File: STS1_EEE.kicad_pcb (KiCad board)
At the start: 4 copper layers, 81.1 x 85 mm, 51 parts, among them J1 2477, U1 coordinate_system, U10 ST_Logo, U2 MP28167GQ

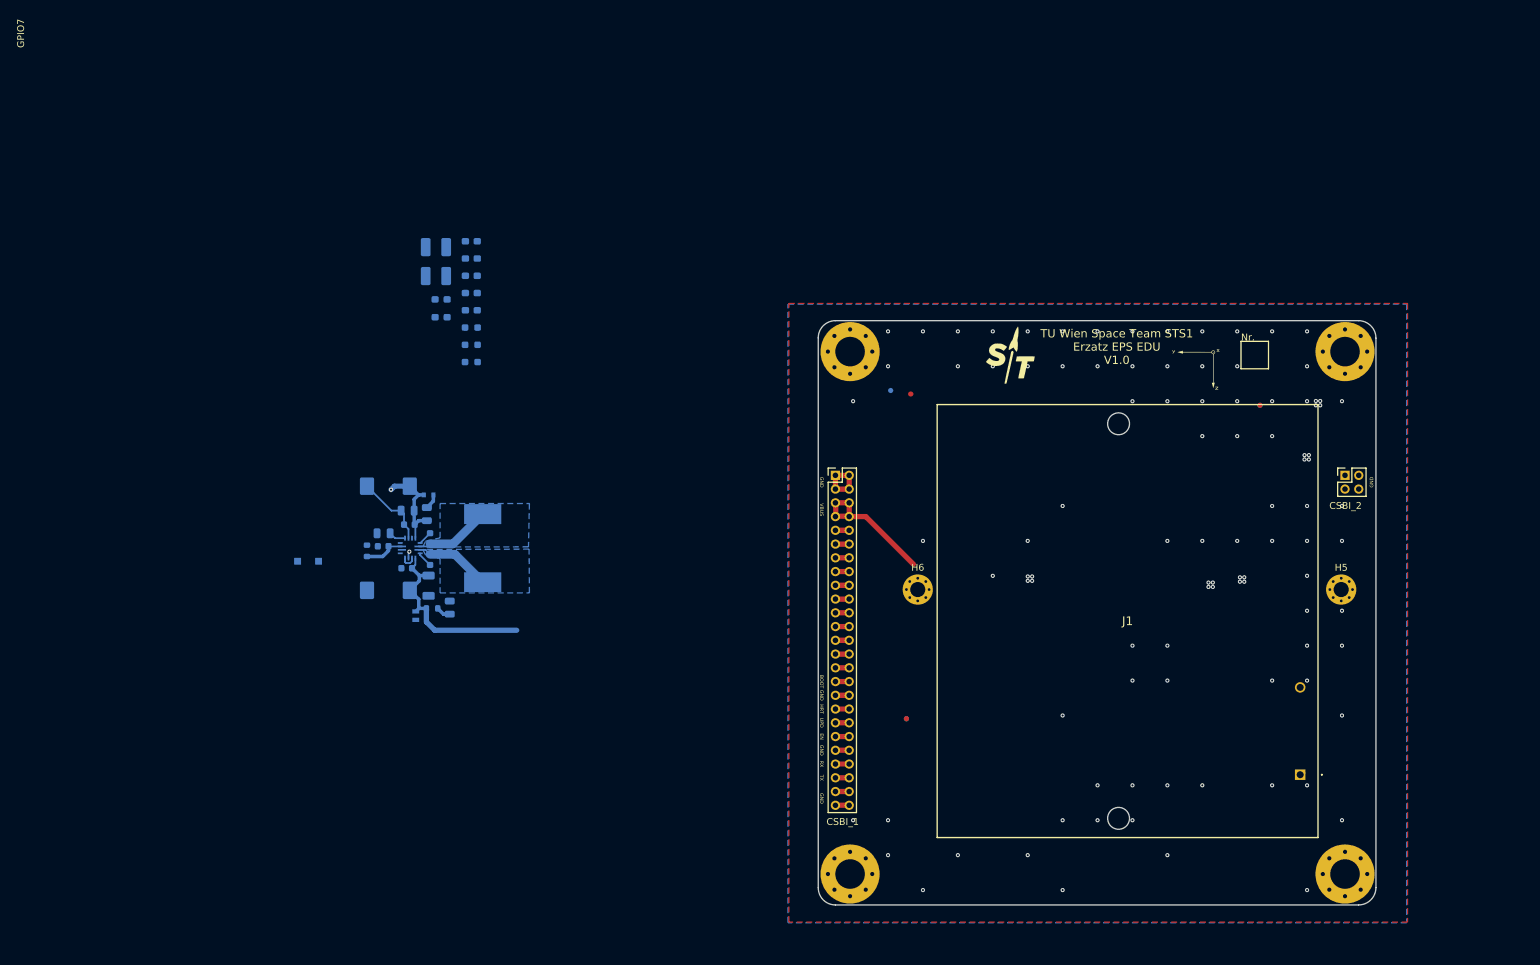
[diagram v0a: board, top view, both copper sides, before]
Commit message: Add 3V3 LDO: could be used to set EPS_BAT_GOOD high
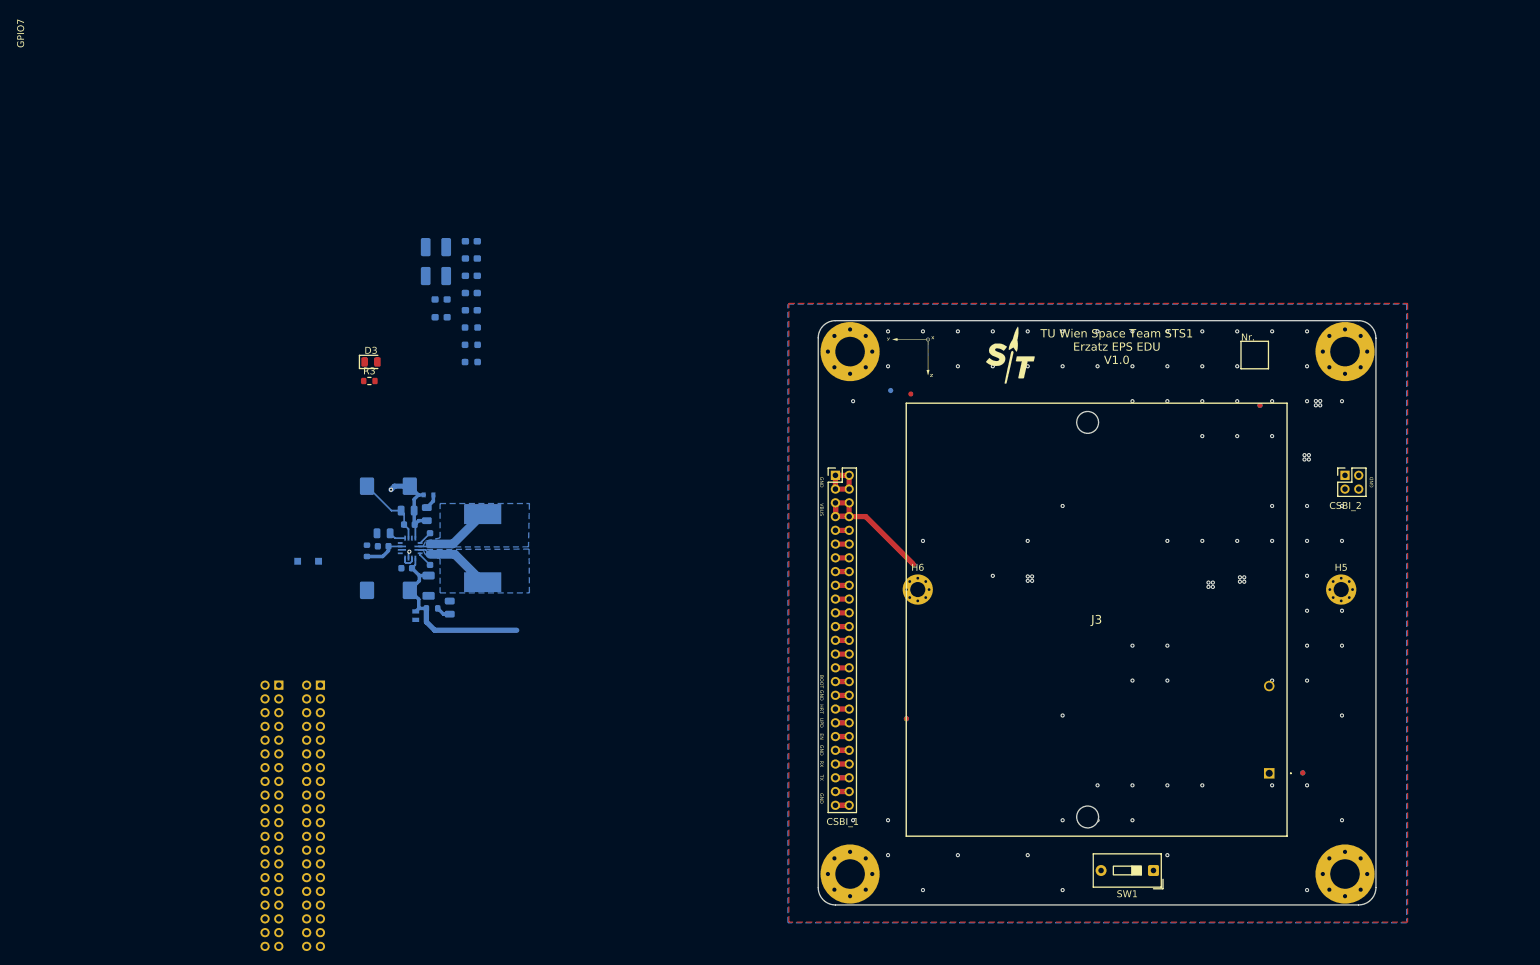
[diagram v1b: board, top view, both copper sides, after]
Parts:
- added D3: LED, LED_SMD:LED_0805_2012Metric, F.Cu at (50.9, 47.8)
- added J2: Conn_02x20_Odd_Even, Connector_PinHeader_2.00mm:PinHeader_2x20_P2.00mm_Vertical, B.Cu at (37.5, 94.8)
- added J3: 2477, STS_EEE:2477, F.Cu at (181.6, 107.7)
- added R3: 220, Resistor_SMD:R_0603_1608Metric, F.Cu at (50.7, 50.6)
- added SW1: SW_SPST, Button_Switch_THT:SW_DIP_SPSTx01_Slide_9.78x4.72mm_W7.62mm_P2.54mm, F.Cu at (164.8, 121.8)
- J1: value 2477 -> Conn_02x20_Odd_Even; footprint STS_EEE:2477 -> Connector_PinHeader_2.00mm:PinHeader_2x20_P2.00mm_Vertical; moved to B.Cu
- moved J1 143.1 mm to (43.6, 94.8), turned to 180 degrees
- moved U1 41.5 mm to (129.5, 46.8)
- renumbered C5 to C1, C14 to C10, C15 to C11, C16 to C12, C6 to C2, C7 to C3, C8 to C4, C9 to C5, C10 to C6, C11 to C7, C12 to C8, C13 to C9, D3 to D1, D4 to D2, D5 to D4, D6 to D5, FID5 to FID2, FID2 to FID3, FID6 to FID4, FID3 to FID5, FID7 to FID6, FID4 to FID7, R11 to R1, R12 to R2, R14 to R4, R15 to R5, U10 to U2, U2 to U3
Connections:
- J1 pad 2: unconnected-(J1---Pad2) -> 3V3

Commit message: Clean-up
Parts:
- removed H5, H6: MountingHole_Pad, MountingHole:MountingHole_2.2mm_M2_Pad_Via
- added C13: 4.7u, Capacitor_SMD:C_0603_1608Metric, F.Cu at (93.0, 63.4)
- added D23: PTVS3V3S1UR,115, Diode_SMD:D_SOD-123, F.Cu at (93.9, 60.5)
- added U4: MCP1725-3302E_MC, STS_EEE:MCP1725-3302E&slash_MC, F.Cu at (75.0, 101.1)
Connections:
- J1 pad 2: 3V3 -> Pi_3V3
- J2 pad 18: 3V3 -> Pi_3V3
- J2 pad 2: 3V3 -> Pi_3V3

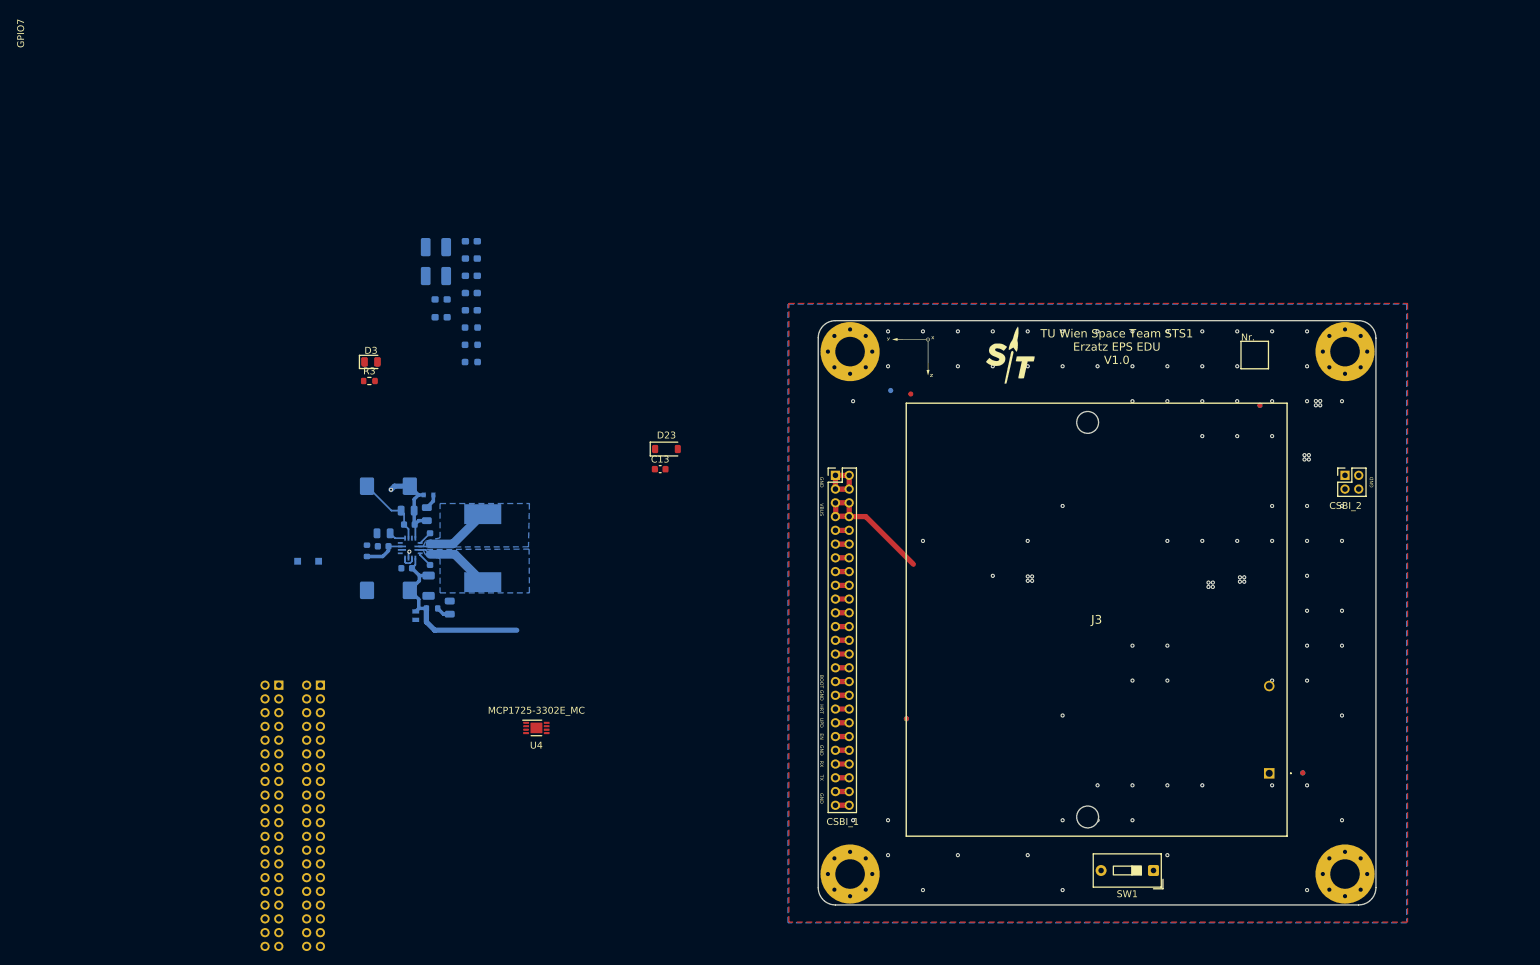
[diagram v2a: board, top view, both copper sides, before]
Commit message: Replace AA battery holder with 18650 one
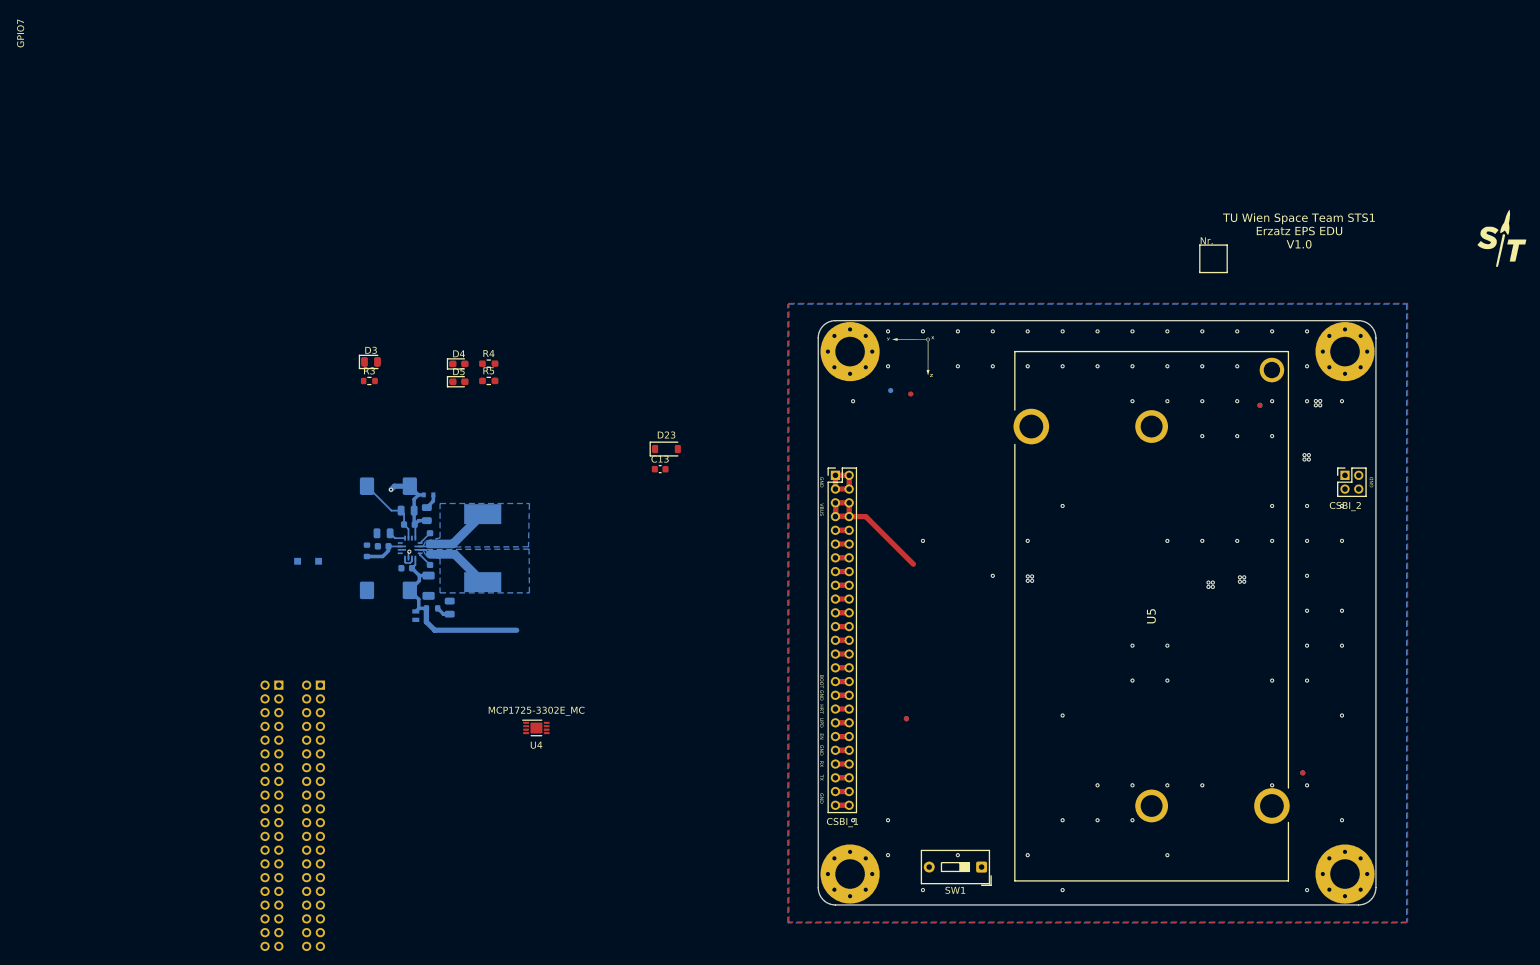
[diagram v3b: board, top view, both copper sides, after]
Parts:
- removed C17: 100n, Capacitor_SMD:C_0603_1608Metric_Pad1.08x0.95mm_HandSolder
- removed C18, C19, C20, C21: 10u, Capacitor_SMD:C_0603_1608Metric_Pad1.08x0.95mm_HandSolder
- removed J3: 2477, STS_EEE:2477
- removed L2, L3: 4.7uH, Inductor_SMD:L_1210_3225Metric_Pad1.42x2.65mm_HandSolder
- removed R13: 100k, Resistor_SMD:R_0603_1608Metric_Pad0.98x0.95mm_HandSolder
- added U5: 1047, STS_EEE:1047, F.Cu at (164.5, 84.8)
- D4, D5, R4, R5: moved to F.Cu
- moved U2 73.5 mm to (215.5, 29.8)
- moved SW1 25.0 mm to (139.8, 121.3)
- moved D5 9.73 mm to (63.7, 50.7), turned to 0 degrees
- moved D4 9.73 mm to (63.7, 48.1), turned to 0 degrees
- moved R4 3.74 mm to (68.1, 48.1), turned to 0 degrees
- moved R5 3.74 mm to (68.1, 50.6), turned to 0 degrees

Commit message: Position PiHat, Raspberry Zero, and battery holder
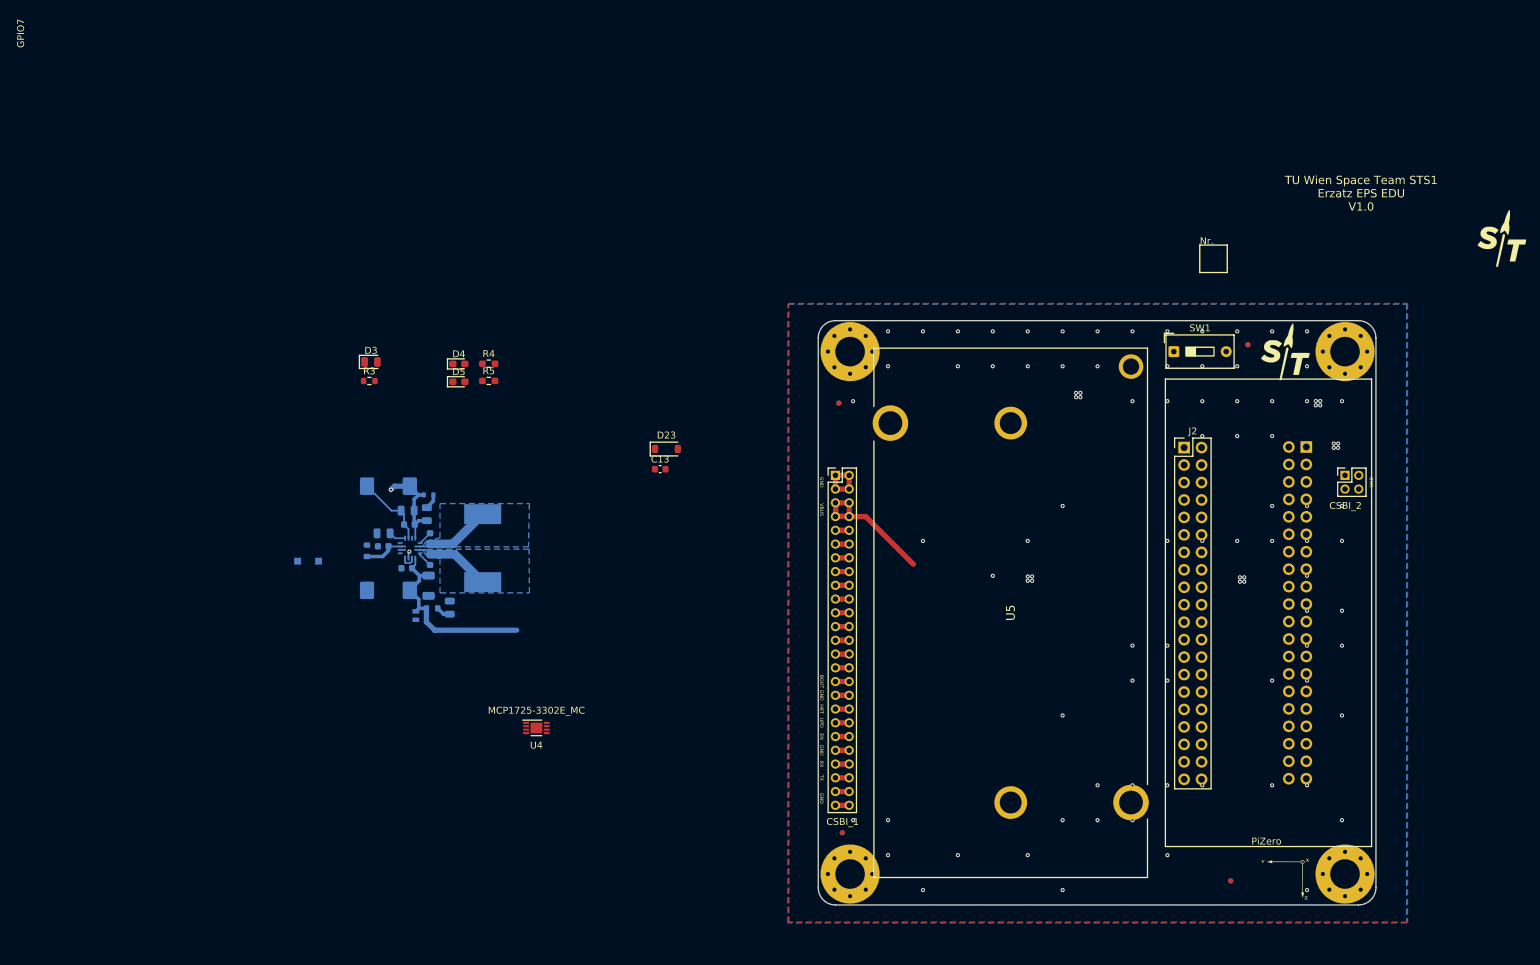
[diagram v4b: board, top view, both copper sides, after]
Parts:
- added U2: ST_Logo, STS_Logo:STLogo_7x8, F.Cu at (184.0, 46.3)
- J1: footprint Connector_PinHeader_2.00mm:PinHeader_2x20_P2.00mm_Vertical -> Connector_PinHeader_2.54mm:PinHeader_2x20_P2.54mm_Vertical
- J2: footprint Connector_PinHeader_2.00mm:PinHeader_2x20_P2.00mm_Vertical -> Connector_PinHeader_2.54mm:PinHeader_2x20_P2.54mm_Vertical; moved to F.Cu
- moved J1 147.6 mm to (187.0, 60.2)
- moved J2 136.2 mm to (169.2, 60.3), turned to 0 degrees
- moved U1 93.5 mm to (184.0, 122.8)
- moved SW1 80.0 mm to (167.7, 46.3), turned to 0 degrees
- moved U5 20.5 mm to (144.0, 84.3)
- moved FID2 19.0 mm to (119.5, 116.3)
- moved FID7 19.0 mm to (119.5, 116.3)
- moved FID1 18.9 mm to (176.0, 123.3)
- moved FID8 18.9 mm to (176.0, 123.3)
- moved FID5 10.5 mm to (119.0, 53.8)
- moved FID3 8.99 mm to (178.5, 45.3)
- moved FID4 8.99 mm to (178.5, 45.3)
- moved FID6 7.76 mm to (119.0, 53.8)
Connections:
- C1 pad 1: VBUS -> VBAT
- C10 pad 1: 5V -> VBUS
- C11 pad 1: 5V -> VBUS
- C12 pad 1: 5V -> VBUS
- C2 pad 1: VBUS -> VBAT
- C3 pad 1: VBUS -> VBAT
- C9 pad 1: 5V -> VBUS
- D1 pad 1: VBUS -> VBAT
- D2 pad 1: 5V -> VBUS
- J2 pad 1: 5V -> VBUS
- J2 pad 3: 5V -> VBUS
- R1 pad 1: VBUS -> VBAT
- R3 pad 1: VBUS -> VBAT
- R5 pad 1: 5V -> VBUS
- SW1 pad 2: VBUS -> VBAT
- U3 pad 1: VBUS -> VBAT
- U3 pad 12: 5V -> VBUS
- U5 pad 4: unconnected-(U5-Pad4) -> GND
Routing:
- net VBAT: track 0.00 -> 27.8 mm
- net 5V: track 14.1 -> 0.00 mm, vias 1 -> 0
- net VBUS: track 48.0 -> 34.3 mm, vias 0 -> 1
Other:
- board text added: "PiHAT"
- board text added: "PiZero"
